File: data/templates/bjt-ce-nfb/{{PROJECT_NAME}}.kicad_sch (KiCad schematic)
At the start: 14 parts, among them Q1 Q2N3904

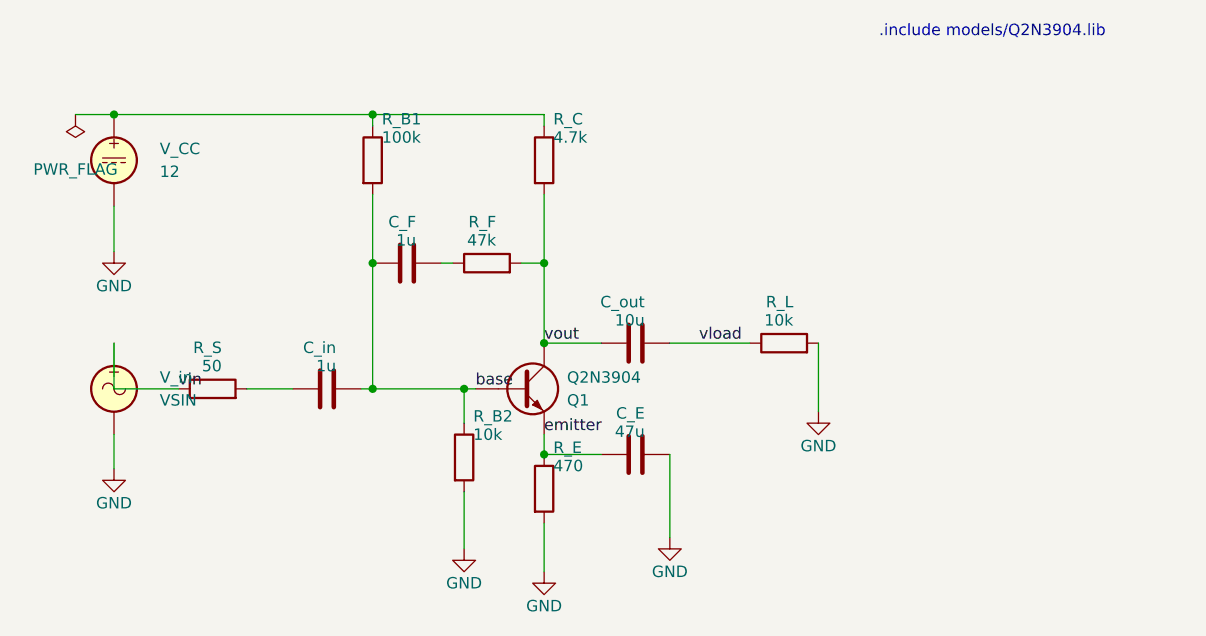
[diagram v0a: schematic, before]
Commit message: T163 fixup: swap R_F/C_F positions in builder for canonical (vout, C_F)
Smoke S7+S8 на materialized fixture (Level 3) обнажили documentation
drift: builder placed C_F at base-side, R_F at vout-side, что не
matches inline calibration test + KB convention `(vout, C_F)`. Agent
correctly identified mismatch и использовал `(vout, R_F)` — same
physics, same PM result — но canonical break ref был неправильный
относительно документации.

Fix: swap _R_F_AT (now X=82.55, base-side) ↔ _C_F_AT (now X=91.44,
vout-side). Connection chain становится base — R_F — fb_mid — C_F —
collector, matching:
- Inline calibration netlist (vout C_F fb_mid R_F base)
- KB topic spice.feedback-break-point.md canonical `(vout, C_F)`
- Tube NFB analog `(sec_a, C_fb)` где DC-block прямо за active output

Verification:
- 3 fixture tests still pass (Q-point invariant к R/C order — same
  electrical топология, разные visual positions).
- 5 calibration tests still pass (inline netlist не зависит от
  KiCad builder).
- Re-bake template + re-build efactory:linux image.
- Re-run smoke S7v2 на новом fixture: PM=126.28° / fc=298.77 Hz @
  canonical (vout, C_F) method=middlebrook_voltage ✓ — strict match
  ADR-T163 ground truth, теперь element_ref=C_F работает напрямую.

Pre-push 5/5 ✓: 1674 passed @ 86.08% coverage (без изменений vs T163
main commit — fixture electrical топология identical, code paths
unchanged).

Co-Authored-By: Claude Opus 4.7 (1M context) <noreply@anthropic.com>
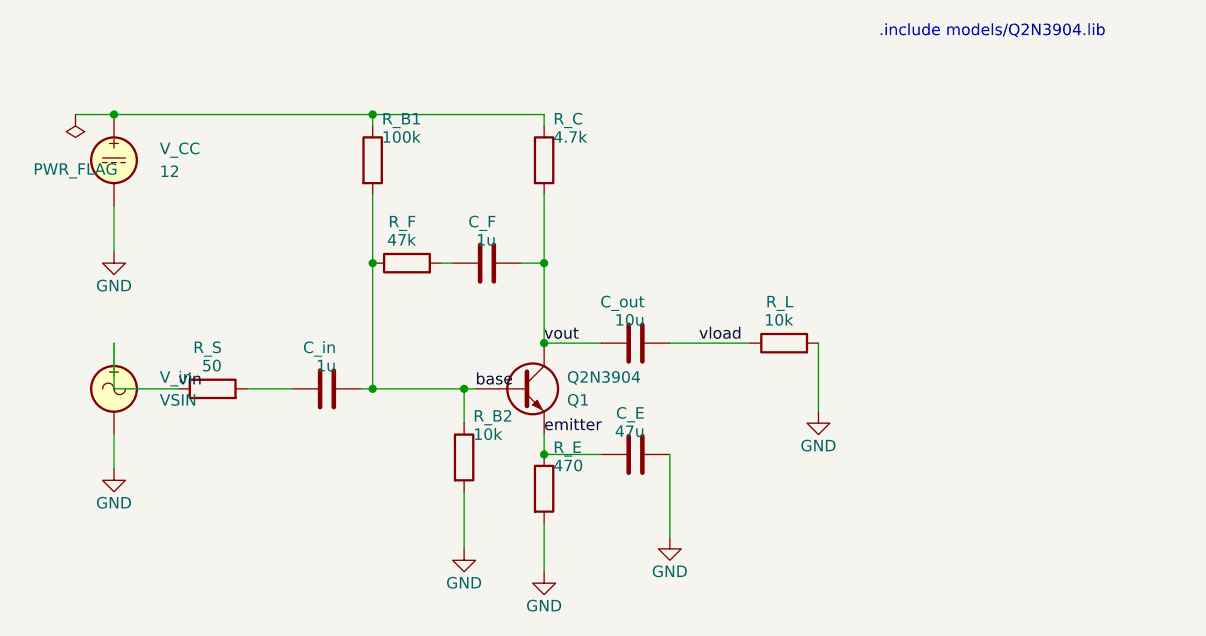
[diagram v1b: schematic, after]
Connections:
- net base: now also R_F.1; no longer C_F.1
- net vout: now also C_F.2; no longer R_F.2
- new net: C_F.1, R_F.2
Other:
- moved on the sheet: C_F, R_F
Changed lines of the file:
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@@
 	(symbol
 		(lib_id "Device:C")
+		(at 91.44 74.93 90)
+		(unit 1)
+		(body_style 1)
+		(exclude_from_sim no)
+		(in_bom yes)
+		(on_board yes)
+		(in_pos_files yes)
+		(dnp no)
+		(fields_autoplaced yes)
+		(property "Reference" "C_F"
+			(at 92.46 70.36 90)
+			(show_name no)
+			(do_not_autoplace no)
+			(effects
+				(font
+					(size 1.27 1.27)
+				)
+				(justify left)
+			)
+		)
+		(property "Value" "1u"
+			(at 92.46 72.39 90)
+			(show_name no)
+			(do_not_autoplace no)
+			(effects
+				(font
+					(size 1.27 1.27)
+				)
+				(justify left)
+			)
+		)
+		(property "Footprint" ""
+			(at 91.44 74.93 0)
+			(hide yes)
+			(show_name no)
+			(do_not_autoplace no)
+			(effects
+				(font
+					(size 1.27 1.27)
+				)
+			)
+		)
+		(property "Datasheet" ""
+			(at 91.44 74.93 0)
+			(hide yes)
+			(show_name no)
+			(do_not_autoplace no)
+			(effects
+				(font
+					(size 1.27 1.27)
+				)
+			)
+		)
+		(property "Description" ""
+			(at 91.44 74.93 0)
+			(hide yes)
+			(show_name no)
+			(do_not_autoplace no)
+			(effects
+				(font
+					(size 1.27 1.27)
+				)
+			)
+		)
+		(pin "1"
+		)
+		(pin "2"
+		)
+		(instances
+			(project "bjt_ce_nfb"
+				(path "/eb433a43-fb04-477d-8088-5e6d4d1cfe14"
+					(reference "C_F")
+					(unit 1)
+				)
+			)
+		)
+	)
+	(symbol
+		(lib_id "Device:R")
 		(at 82.55 74.93 90)
 		(unit 1)
@@
 		(dnp no)
 		(fields_autoplaced yes)
-		(property "Reference" "C_F"
+		(property "Reference" "R_F"
 			(at 83.57 70.36 90)
 			(show_name no)
@@
 			)
 		)
-		(property "Value" "1u"
+		(property "Value" "47k"
 			(at 83.57 72.39 90)
 			(show_name no)
@@
 			(hide yes)
 			(show_name no)
-			(do_not_autoplace no)
-			(effects
-				(font
-					(size 1.27 1.27)
-				)
-			)
-		)
-		(pin "1"
-		)
-		(pin "2"
-		)
-		(instances
-			(project "bjt_ce_nfb"
-				(path "/eb433a43-fb04-477d-8088-5e6d4d1cfe14"
-					(reference "C_F")
-					(unit 1)
-				)
-			)
-		)
-	)
-	(symbol
-		(lib_id "Device:R")
-		(at 91.44 74.93 90)
-		(unit 1)
-		(body_style 1)
-		(exclude_from_sim no)
-		(in_bom yes)
-		(on_board yes)
-		(in_pos_files yes)
-		(dnp no)
-		(fields_autoplaced yes)
-		(property "Reference" "R_F"
-			(at 92.46 70.36 90)
-			(show_name no)
-			(do_not_autoplace no)
-			(effects
-				(font
-					(size 1.27 1.27)
-				)
-				(justify left)
-			)
-		)
-		(property "Value" "47k"
-			(at 92.46 72.39 90)
-			(show_name no)
-			(do_not_autoplace no)
-			(effects
-				(font
-					(size 1.27 1.27)
-				)
-				(justify left)
-			)
-		)
-		(property "Footprint" ""
-			(at 91.44 74.93 0)
-			(hide yes)
-			(show_name no)
-			(do_not_autoplace no)
-			(effects
-				(font
-					(size 1.27 1.27)
-				)
-			)
-		)
-		(property "Datasheet" ""
-			(at 91.44 74.93 0)
-			(hide yes)
-			(show_name no)
-			(do_not_autoplace no)
-			(effects
-				(font
-					(size 1.27 1.27)
-				)
-			)
-		)
-		(property "Description" ""
-			(at 91.44 74.93 0)
-			(hide yes)
-			(show_name no)

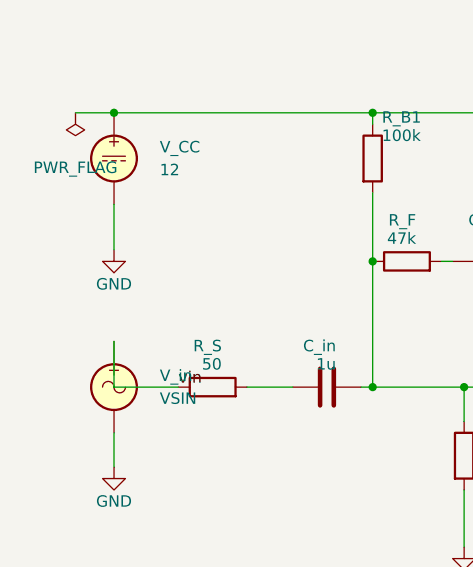
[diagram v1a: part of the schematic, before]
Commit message: T029 Phase 0: fix 4 dirty templates via builders
Builders (active-lpf-sallen-key, op-amp-inverting, bjt-ce-nfb) add a
PWR_FLAG on the GND net to clear ERC `power_pin_not_driven`. The
tube-line-preamp builder fixes r_g2.pin_b wiring — previous connect
target (114.3, 90.17) was the pin's own coordinate (zero-length wire),
leaving R4 pin 1 floating; new target (114.3, 88.9) places it on the
grid2 net as a canonical grid-leak.

data/templates/* regenerated via scripts/regenerate-templates.py. All
11 templates now ERC-clean (errors=0) — satisfies T029 SC1.

Calibration baselines for tube-line-preamp updated to reflect the now
correctly-biased CF: V_cathode2 window 30-150V → 2-50V; mid-band gain
baseline 64.0 → 54.0 V/V (matches analytical 54 V/V hand-calc exactly,
which is now achievable because R4 grid-leak loads C3→V1B coupling per
hand-calc assumption).

Spec §6 A1 amended: fix path is "via builders + regen", not direct
edits to data/templates/. Direct-edit probe (2026-06-05) confirmed
0-errors achievable but breaks snapshot tests and is wiped by next
regenerate-templates.py.

Pre-push 5/5 ✓ (ruff/format/mypy clean; 2025 passed, 10 skipped,
1 xfailed; coverage 86.98%).

Co-Authored-By: Claude Opus 4.7 (1M context) <noreply@anthropic.com>
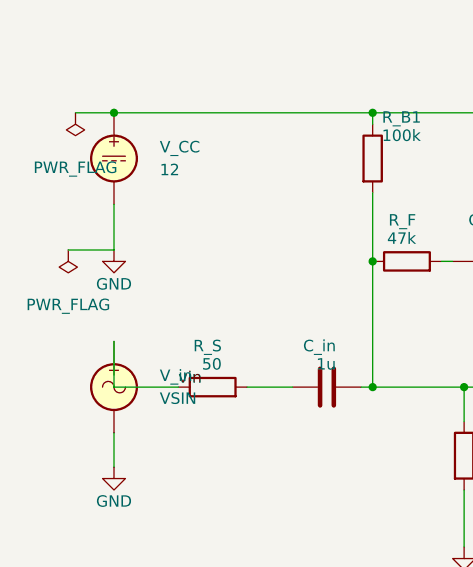
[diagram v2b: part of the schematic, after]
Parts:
- removed R_S: 50, symbol Device:R
- added Q1: Q2N3904, symbol Device:Q_NPN
- C_E: renamed from C_out; value 10u -> 47u
- C_F: renamed from R_F; value 47k -> 1u; symbol Device:R -> Device:C
- C_in: renamed from R_B1; value 100k -> 1u; symbol Device:R -> Device:C
- C_out: renamed from R_L; value 10k -> 10u; symbol Device:R -> Device:C
- R_B1: renamed from R_B2; value 10k -> 100k
- R_B2: renamed from C_F; value 1u -> 10k; symbol Device:C -> Device:R
- R_C: renamed from R_E; value 470 -> 4.7k
- R_E: renamed from C_E; value 47u -> 470; symbol Device:C -> Device:R
- R_F: renamed from R_C; value 4.7k -> 47k
- R_L: renamed from Q1; value Q2N3904 -> 10k; symbol Device:Q_NPN -> Device:R
- R_S: renamed from C_in; value 1u -> 50; symbol Device:C -> Device:R
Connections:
- net GND: now also C_E.2, R_B2.2, R_L.2; no longer C_out.2, R_B1.2, R_C.2
- net base: now also R_B1.2, R_B2.1, R_F.1, Q1.B; no longer C_F.1, R_B1.1, R_L.B, R_S.2
- net emitter: now also C_E.1, Q1.E; no longer R_C.1, R_L.E
- net vin: now also R_S.1
- net vload: now also C_out.2, R_L.1; no longer C_E.2, C_out.1
- net vout: now also C_F.2, C_out.1, R_C.2, Q1.C; no longer C_E.1, R_B2.2, R_F.2, R_L.C
- new net: C_F.1, R_F.2
- new net: R_B1.1, R_C.1, V_CC.1
- new net: C_in.1, R_S.2
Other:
- moved on the sheet: C_E, R_B1, R_C, R_F
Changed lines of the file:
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@@
+	(wire
+		(pts
+			(xy 44.92 73.66) (xy 50 73.66)
+		)
+		(stroke
+			(width 0)
+			(type default)
+		)
+	)
 	(wire
 		(pts
@@
 					(unit 1)
 				)
+			)
+		)
+	)
+	(symbol
+		(lib_id "power:PWR_FLAG")
+		(at 44.92 73.66 180)
+		(unit 1)
+		(body_style 1)
+		(exclude_from_sim no)
+		(in_bom yes)
+		(on_board yes)
+		(in_pos_files yes)
+		(dnp no)
+		(fields_autoplaced yes)
+		(property "Reference" "#FLG02"
+			(at 44.92 71.76 0)
+			(hide yes)
+			(show_name no)
+			(do_not_autoplace no)
+			(effects
+				(font
+					(size 1.27 1.27)
+				)
+			)
+		)
+		(property "Value" "PWR_FLAG"
+			(at 44.92 79.76 0)
+			(show_name no)
+			(do_not_autoplace no)
+			(effects
+				(font
+					(size 1.27 1.27)
+				)
+			)
+		)
+		(property "Footprint" ""
+			(at 44.92 73.66 0)
+			(show_name no)
+			(do_not_autoplace no)
+			(effects
+				(font
+					(size 1.27 1.27)
+				)
+			)
+		)
+		(property "Datasheet" ""
+			(at 44.92 73.66 0)
+			(show_name no)
+			(do_not_autoplace no)
+			(effects
+				(font
+					(size 1.27 1.27)
+				)
+			)
+		)
+		(property "Description" ""
+			(at 44.92 73.66 0)
+			(hide yes)
+			(show_name no)
+			(do_not_autoplace no)
+			(effects
+				(font
+					(size 1.27 1.27)
+				)
+			)
+		)
+		(pin "1"
+		)
+		(instances
+			(project "bjt_ce_nfb"
+				(path "/eb433a43-fb04-477d-8088-5e6d4d1cfe14"
+					(reference "#FLG02")
+					(unit 1)
+				)
